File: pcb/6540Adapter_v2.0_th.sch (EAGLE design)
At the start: 8 parts, among them IC1 6540, IC2 2716 - 27512, IC3 74LS138N

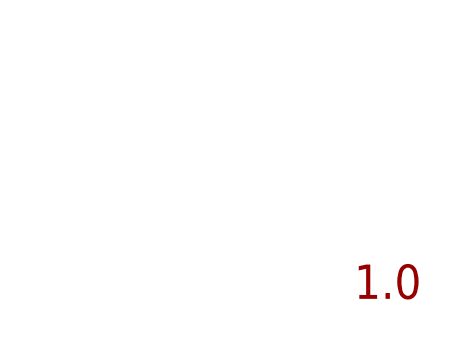
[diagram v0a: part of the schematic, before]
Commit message: PCB Updates and BOM cleanup
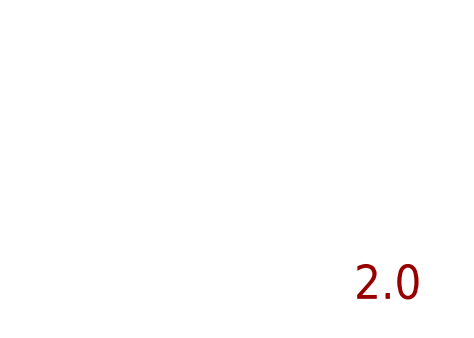
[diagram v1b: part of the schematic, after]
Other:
- note added: "2.0"
- note removed: "1.0"
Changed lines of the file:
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@@
 <?xml version="1.0" encoding="utf-8"?>
 <!DOCTYPE eagle SYSTEM "eagle.dtd">
-<eagle version="7.6.0">
+<eagle version="7.7.0">
 <drawing>
 <settings>
@@
 <plain>
 <text x="165.1" y="25.4" size="5.08" layer="94">6540 ROM-el</text>
-<text x="252.222" y="6.096" size="3.81" layer="94">1.0</text>
+<text x="252.222" y="6.096" size="3.81" layer="94">2.0</text>
 </plain>
 <instances>
